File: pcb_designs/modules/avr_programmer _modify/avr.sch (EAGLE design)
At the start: 17 parts, among them IC1 QT9701BD, Q1 12 MHZ

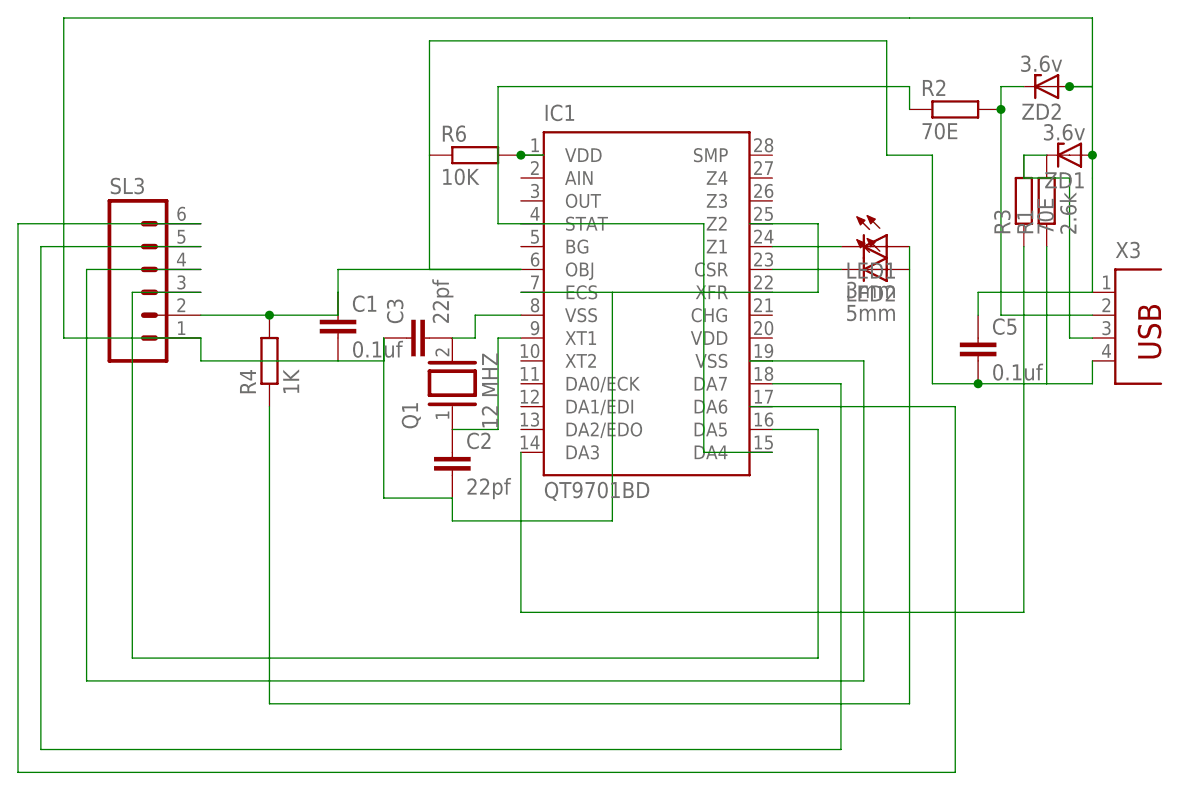
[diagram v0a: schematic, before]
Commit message: 
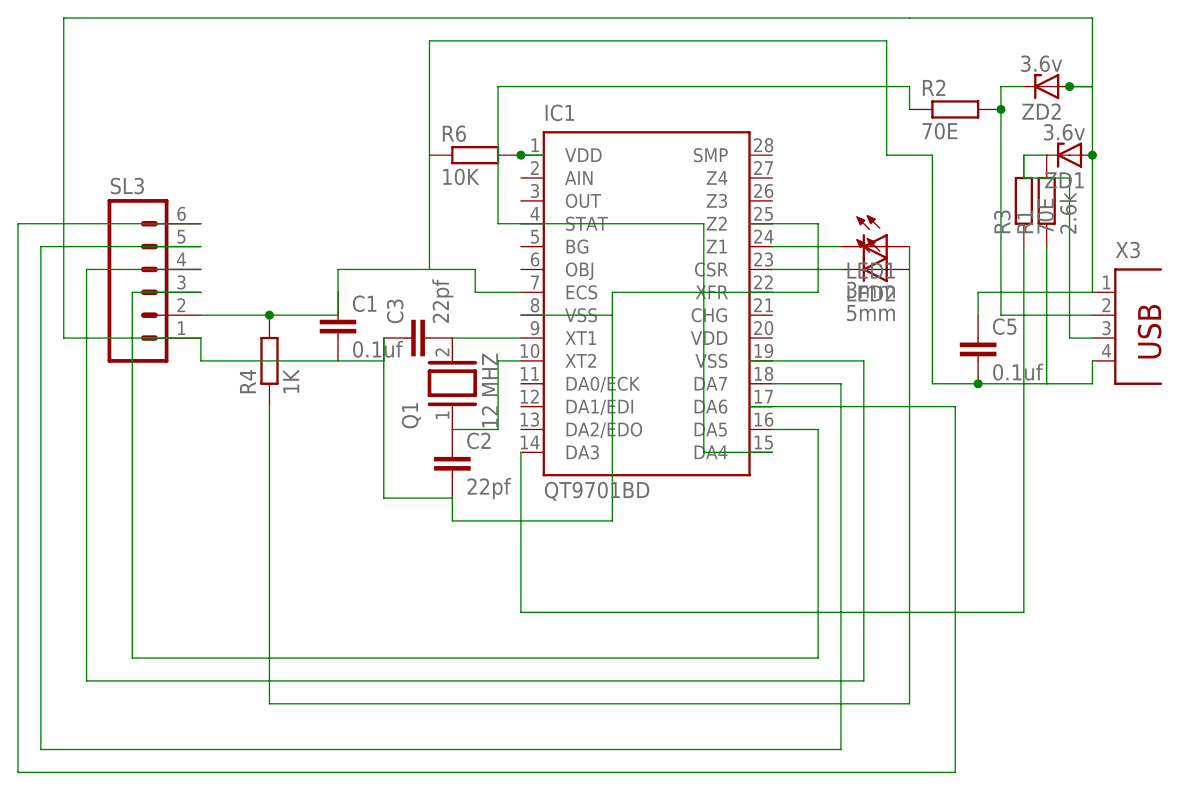
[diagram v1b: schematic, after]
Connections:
- removed net N$7: C1.1, C5.2, IC1.OBJ, R1.1, R4.2, R6.1, SL3.2, X3.4
- new net N$17: C1.1, C5.2, IC1.ECS, R1.1, R4.2, R6.1, SL3.2, X3.4
- net N$1: now also IC1.XT1; no longer IC1.VSS
- net N$2: now also IC1.XT2; no longer IC1.XT1
- net N$3: now also IC1.VSS; no longer IC1.ECS
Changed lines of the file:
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@@
 <?xml version="1.0" encoding="utf-8"?>
 <!DOCTYPE eagle SYSTEM "eagle.dtd">
-<eagle version="6.5.0">
+<eagle version="6.1">
 <drawing>
 <settings>
@@
 <pinref part="Q1" gate="G$1" pin="2"/>
 <pinref part="C3" gate="G$1" pin="2"/>
-<wire x1="38.1" y1="66.04" x2="40.64" y2="66.04" width="0.1524" layer="91"/>
-<wire x1="40.64" y1="66.04" x2="40.64" y2="68.58" width="0.1524" layer="91"/>
-<pinref part="IC1" gate="G$1" pin="VSS"/>
-<wire x1="40.64" y1="68.58" x2="45.72" y2="68.58" width="0.1524" layer="91"/>
+<pinref part="IC1" gate="G$1" pin="XT1"/>
+<wire x1="38.1" y1="66.04" x2="45.72" y2="66.04" width="0.1524" layer="91"/>
 </segment>
 </net>
@@
 <pinref part="C2" gate="G$1" pin="1"/>
 <wire x1="38.1" y1="55.88" x2="43.18" y2="55.88" width="0.1524" layer="91"/>
-<wire x1="43.18" y1="55.88" x2="43.18" y2="66.04" width="0.1524" layer="91"/>
-<pinref part="IC1" gate="G$1" pin="XT1"/>
-<wire x1="43.18" y1="66.04" x2="45.72" y2="66.04" width="0.1524" layer="91"/>
+<wire x1="43.18" y1="55.88" x2="43.18" y2="63.5" width="0.1524" layer="91"/>
+<pinref part="IC1" gate="G$1" pin="XT2"/>
+<wire x1="43.18" y1="63.5" x2="45.72" y2="63.5" width="0.1524" layer="91"/>
 </segment>
 </net>
@@
 <net name="N$3" class="0">
 <segment>
-<pinref part="IC1" gate="G$1" pin="ECS"/>
-<wire x1="45.72" y1="71.12" x2="55.88" y2="71.12" width="0.1524" layer="91"/>
-<wire x1="55.88" y1="71.12" x2="55.88" y2="45.72" width="0.1524" layer="91"/>
+<wire x1="55.88" y1="71.12" x2="55.88" y2="68.58" width="0.1524" layer="91"/>
 <pinref part="C2" gate="G$1" pin="2"/>
+<wire x1="55.88" y1="68.58" x2="55.88" y2="45.72" width="0.1524" layer="91"/>
 <wire x1="55.88" y1="45.72" x2="38.1" y2="45.72" width="0.1524" layer="91"/>
 <wire x1="38.1" y1="45.72" x2="38.1" y2="48.26" width="0.1524" layer="91"/>
@@
 <wire x1="109.22" y1="71.12" x2="96.52" y2="71.12" width="0.1524" layer="91"/>
 <wire x1="96.52" y1="71.12" x2="96.52" y2="68.58" width="0.1524" layer="91"/>
+<pinref part="IC1" gate="G$1" pin="VSS"/>
+<wire x1="45.72" y1="68.58" x2="55.88" y2="68.58" width="0.1524" layer="91"/>
 </segment>
 </net>
@@
 </segment>
 </net>
-<net name="N$7" class="0">
+<net name="N$9" class="0">
+<segment>
+<pinref part="ZD1" gate="1" pin="C"/>
+<pinref part="R1" gate="G$1" pin="2"/>
+<pinref part="X3" gate="G$1" pin="3"/>
+<wire x1="109.22" y1="66.04" x2="106.68" y2="66.04" width="0.1524" layer="91"/>
+<wire x1="106.68" y1="66.04" x2="106.68" y2="83.82" width="0.1524" layer="91"/>
+<pinref part="R3" gate="G$1" pin="2"/>
+<wire x1="106.68" y1="83.82" x2="101.6" y2="83.82" width="0.1524" layer="91"/>
+<wire x1="101.6" y1="83.82" x2="101.6" y2="86.36" width="0.1524" layer="91"/>
+<wire x1="101.6" y1="86.36" x2="104.14" y2="86.36" width="0.1524" layer="91"/>
+</segment>
+</net>
+<net name="N$11" class="0">
+<segment>
+<pinref part="IC1" gate="G$1" pin="DA3"/>
+<wire x1="45.72" y1="53.34" x2="45.72" y2="35.56" width="0.1524" layer="91"/>
+<pinref part="R3" gate="G$1" pin="1"/>
+<wire x1="45.72" y1="35.56" x2="101.6" y2="35.56" width="0.1524" layer="91"/>
+<wire x1="101.6" y1="35.56" x2="101.6" y2="76.2" width="0.1524" layer="91"/>
+</segment>
+</net>
+<net name="N$10" class="0">
+<segment>
+<pinref part="R4" gate="G$1" pin="1"/>
+<wire x1="17.78" y1="58.42" x2="17.78" y2="25.4" width="0.1524" layer="91"/>
+<pinref part="LED2" gate="G$1" pin="A"/>
+<wire x1="17.78" y1="25.4" x2="88.9" y2="25.4" width="0.1524" layer="91"/>
+<wire x1="88.9" y1="25.4" x2="88.9" y2="73.66" width="0.1524" layer="91"/>
+<pinref part="LED1" gate="G$1" pin="A"/>
+<wire x1="88.9" y1="73.66" x2="88.9" y2="76.2" width="0.1524" layer="91"/>
+</segment>
+</net>
+<net name="N$14" class="0">
+<segment>
+<pinref part="IC1" gate="G$1" pin="DA5"/>
+<wire x1="73.66" y1="55.88" x2="78.74" y2="55.88" width="0.1524" layer="91"/>
+<wire x1="78.74" y1="55.88" x2="78.74" y2="30.48" width="0.1524" layer="91"/>
+<wire x1="78.74" y1="30.48" x2="2.54" y2="30.48" width="0.1524" layer="91"/>
+<wire x1="2.54" y1="30.48" x2="2.54" y2="71.12" width="0.1524" layer="91"/>
+<pinref part="SL3" gate="G$1" pin="3"/>
+<wire x1="2.54" y1="71.12" x2="10.16" y2="71.12" width="0.1524" layer="91"/>
+</segment>
+</net>
+<net name="N$15" class="0">
+<segment>
+<pinref part="IC1" gate="G$1" pin="DA7"/>
+<wire x1="73.66" y1="60.96" x2="81.28" y2="60.96" width="0.1524" layer="91"/>
+<wire x1="81.28" y1="60.96" x2="81.28" y2="20.32" width="0.1524" layer="91"/>
+<wire x1="81.28" y1="20.32" x2="-7.62" y2="20.32" width="0.1524" layer="91"/>
+<wire x1="-7.62" y1="20.32" x2="-7.62" y2="76.2" width="0.1524" layer="91"/>
+<pinref part="SL3" gate="G$1" pin="5"/>
+<wire x1="-7.62" y1="76.2" x2="10.16" y2="76.2" width="0.1524" layer="91"/>
+</segment>
+</net>
+<net name="N$17" class="0">
 <segment>
 <pinref part="C1" gate="G$1" pin="1"/>
 <wire x1="25.4" y1="71.12" x2="25.4" y2="73.66" width="0.1524" layer="91"/>
-<pinref part="IC1" gate="G$1" pin="OBJ"/>
-<wire x1="25.4" y1="73.66" x2="45.72" y2="73.66" width="0.1524" layer="91"/>
+<wire x1="25.4" y1="68.58" x2="25.4" y2="71.12" width="0.1524" layer="91"/>
+<wire x1="17.78" y1="68.58" x2="25.4" y2="68.58" width="0.1524" layer="91"/>
+<pinref part="R4" gate="G$1" pin="2"/>
+<junction x="17.78" y="68.58"/>
+<pinref part="SL3" gate="G$1" pin="2"/>
+<wire x1="10.16" y1="68.58" x2="17.78" y2="68.58" width="0.1524" layer="91"/>
 <pinref part="R6" gate="G$1" pin="1"/>
-<wire x1="45.72" y1="73.66" x2="35.56" y2="73.66" width="0.1524" layer="91"/>
 <wire x1="35.56" y1="73.66" x2="35.56" y2="86.36" width="0.1524" layer="91"/>
 <wire x1="35.56" y1="86.36" x2="35.56" y2="99.06" width="0.1524" layer="91"/>
@@
 <pinref part="C5" gate="G$1" pin="2"/>
 <junction x="96.52" y="60.96"/>
-<pinref part="SL3" gate="G$1" pin="2"/>
-<wire x1="10.16" y1="68.58" x2="17.78" y2="68.58" width="0.1524" layer="91"/>
-<wire x1="17.78" y1="68.58" x2="25.4" y2="68.58" width="0.1524" layer="91"/>
-<wire x1="25.4" y1="68.58" x2="25.4" y2="71.12" width="0.1524" layer="91"/>
-<pinref part="R4" gate="G$1" pin="2"/>
-<junction x="17.78" y="68.58"/>
-</segment>
-</net>
-<net name="N$9" class="0">
-<segment>
-<pinref part="ZD1" gate="1" pin="C"/>
-<pinref part="R1" gate="G$1" pin="2"/>
-<pinref part="X3" gate="G$1" pin="3"/>
-<wire x1="109.22" y1="66.04" x2="106.68" y2="66.04" width="0.1524" layer="91"/>
-<wire x1="106.68" y1="66.04" x2="106.68" y2="83.82" width="0.1524" layer="91"/>
-<pinref part="R3" gate="G$1" pin="2"/>
-<wire x1="106.68" y1="83.82" x2="101.6" y2="83.82" width="0.1524" layer="91"/>
-<wire x1="101.6" y1="83.82" x2="101.6" y2="86.36" width="0.1524" layer="91"/>
-<wire x1="101.6" y1="86.36" x2="104.14" y2="86.36" width="0.1524" layer="91"/>
-</segment>
-</net>
-<net name="N$11" class="0">
-<segment>
-<pinref part="IC1" gate="G$1" pin="DA3"/>
-<wire x1="45.72" y1="53.34" x2="45.72" y2="35.56" width="0.1524" layer="91"/>
-<pinref part="R3" gate="G$1" pin="1"/>
-<wire x1="45.72" y1="35.56" x2="101.6" y2="35.56" width="0.1524" layer="91"/>
-<wire x1="101.6" y1="35.56" x2="101.6" y2="76.2" width="0.1524" layer="91"/>
-</segment>
-</net>
-<net name="N$10" class="0">
-<segment>
-<pinref part="R4" gate="G$1" pin="1"/>
-<wire x1="17.78" y1="58.42" x2="17.78" y2="25.4" width="0.1524" layer="91"/>
-<pinref part="LED2" gate="G$1" pin="A"/>
-<wire x1="17.78" y1="25.4" x2="88.9" y2="25.4" width="0.1524" layer="91"/>
-<wire x1="88.9" y1="25.4" x2="88.9" y2="73.66" width="0.1524" layer="91"/>
-<pinref part="LED1" gate="G$1" pin="A"/>
-<wire x1="88.9" y1="73.66" x2="88.9" y2="76.2" width="0.1524" layer="91"/>
-</segment>
-</net>
-<net name="N$14" class="0">
-<segment>
-<pinref part="IC1" gate="G$1" pin="DA5"/>
-<wire x1="73.66" y1="55.88" x2="78.74" y2="55.88" width="0.1524" layer="91"/>
-<wire x1="78.74" y1="55.88" x2="78.74" y2="30.48" width="0.1524" layer="91"/>
-<wire x1="78.74" y1="30.48" x2="2.54" y2="30.48" width="0.1524" layer="91"/>
-<wire x1="2.54" y1="30.48" x2="2.54" y2="71.12" width="0.1524" layer="91"/>
-<pinref part="SL3" gate="G$1" pin="3"/>
-<wire x1="2.54" y1="71.12" x2="10.16" y2="71.12" width="0.1524" layer="91"/>
-</segment>
-</net>
-<net name="N$15" class="0">
-<segment>
-<pinref part="IC1" gate="G$1" pin="DA7"/>
-<wire x1="73.66" y1="60.96" x2="81.28" y2="60.96" width="0.1524" layer="91"/>
-<wire x1="81.28" y1="60.96" x2="81.28" y2="20.32" width="0.1524" layer="91"/>
-<wire x1="81.28" y1="20.32" x2="-7.62" y2="20.32" width="0.1524" layer="91"/>
-<wire x1="-7.62" y1="20.32" x2="-7.62" y2="76.2" width="0.1524" layer="91"/>
-<pinref part="SL3" gate="G$1" pin="5"/>
-<wire x1="-7.62" y1="76.2" x2="10.16" y2="76.2" width="0.1524" layer="91"/>
-</segment>
-</net>
+<wire x1="25.4" y1="73.66" x2="35.56" y2="73.66" width="0.1524" layer="91"/>
+<wire x1="35.56" y1="73.66" x2="40.64" y2="73.66" width="0.1524" layer="91"/>
+<wire x1="40.64" y1="73.66" x2="40.64" y2="71.12" width="0.1524" layer="91"/>
+<pinref part="IC1" gate="G$1" pin="ECS"/>
+<wire x1="40.64" y1="71.12" x2="45.72" y2="71.12" width="0.1524" layer="91"/>
+</segment>
+</net>
